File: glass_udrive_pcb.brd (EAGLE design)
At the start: 8.5 x 19 mm, 20 parts

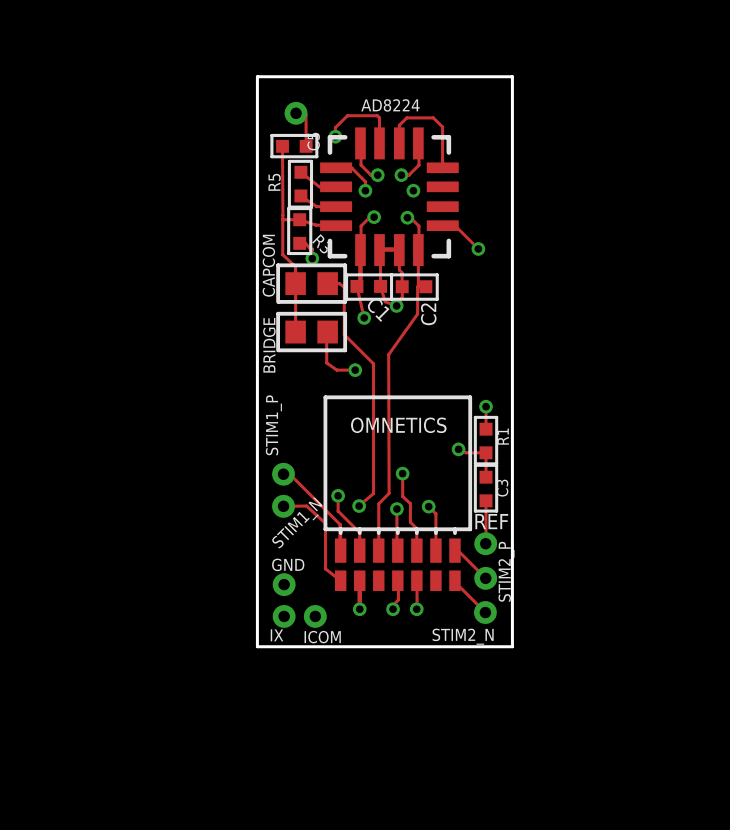
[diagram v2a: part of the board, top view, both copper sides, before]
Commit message: 1-Incorporating Michael Stetner's comments: ====================================================== 1. Move vias carrying output signals away from the corners of the AD8224. According to the datasheet (bottom of p. 22), vias should not be placed under the corners of the chip. 2. If you have enough space, add a 10 uF bypass capacitor on each supply, as suggested by the datasheet. These can be far from the AD8224. 3. Add a through hole for GND. This hole will be used during surgery to solder the ground wire that you put under the bird's skull. You already have one GND through hole, but that will be in use by the motor. 4. Remove the vias for +15V and -15V that are underneath the AD8224. Just run those two of the traces on the top side of the board. 5. Change capacitance of C1-C2 to 0.1 uF, per the datasheet 6. Remove the trace between the reference pads of the AD8224. This creates a loop in your ground, and loops pick up electromagnetic interference. 7. Add an orientation marker for the AD8224 on the silkscreen 8. On the bill of materials, fix the device name for the AD8224 (it says AD8424). 9. Increase the width of the traces for Ix, ICOM, +15V, and -15V. A wider trace will have a lower resistance, which is especially important for these traces that will be carrying the most current. ====================================================== 2-Redesigned and re-routed to match the available componenets' package sizes. 3-Added the headplate structure with thru-holes 4- fixed the dimension layer
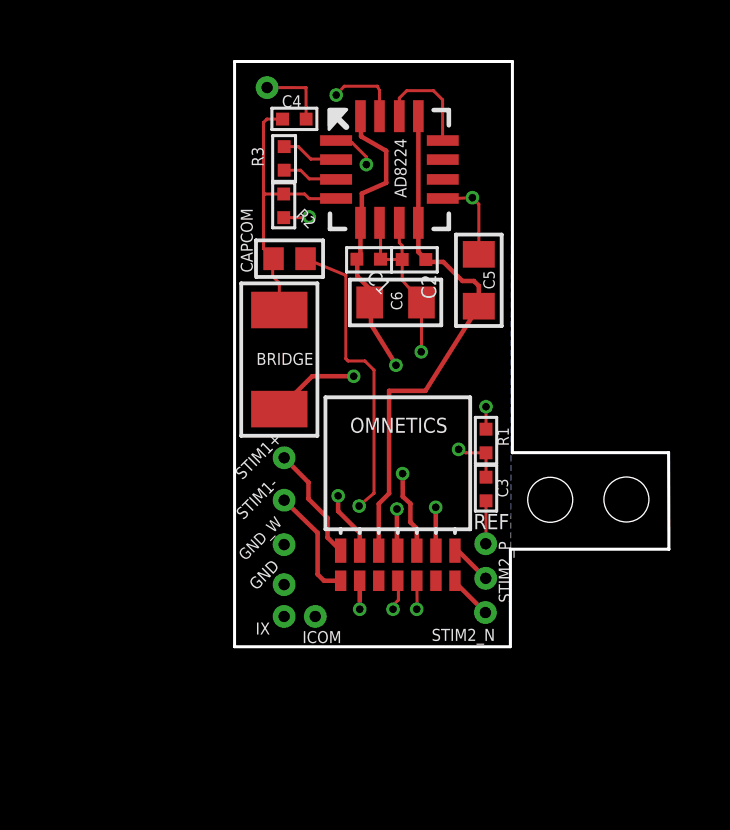
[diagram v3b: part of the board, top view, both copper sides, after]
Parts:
- removed R5: 5.49KOhm, GFL:0201
- removed STIM1_N, STIM1_P: (no value), GFL:30MIL/15MIL
- added C4: 6800pF, GFL:0201
- added C6: 10uF, GFL:0603
- added GND_W, STIM1+, STIM1-: (no value), GFL:30MIL/15MIL
- added R2: 10Mohm, GFL:0201
- BRIDGE: device GFL:0402 -> GFL:1206
- C1, C2: value .01uF -> 0.1uF
- C5: value 6800pF -> 10uF; device GFL:0201 -> GFL:0603
- R3: value 10Mohm -> 5.49KOhm
- moved C5 7.60 mm to (7.38, 12.2), turned to 270 degrees
- moved R3 2.49 mm to (0.89, 16.3)
- moved BRIDGE 1.42 mm to (0.73, 9.57), turned to 270 degrees
- moved GLASS 1.29 mm to (0.32, 18.6)
- moved CAPCOM 1.11 mm to (1.07, 12.9)
- moved AD8224 0.91 mm to (4.40, 15.9)
- moved C1 0.91 mm to (3.71, 12.9)
- moved C2 0.91 mm to (5.22, 12.9)
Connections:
- net +15V: now also C6.2
- net -15V: now also C5.2
- net GLASS: now also C4.1; no longer C5.1
- net GLASS_FLT: now also C4.2, R2.2; no longer C5.2, R3.2
- net GND: now also C5.1, C6.1, GND_W.P$1, R2.1; no longer R3.1
- net N$2: now also R3.2; no longer R5.2
- net N$4: now also R3.1; no longer R5.1
- net STIM1_N: now also STIM1-.P$1; no longer STIM1_N.P$1
- net STIM1_P: now also STIM1+.P$1; no longer STIM1_P.P$1
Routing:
- net GND: track 9.82 -> 13.0 mm
- net -15V: track 15.7 -> 17.7 mm, vias 2 -> 0
- net CAP_COM: track 13.0 -> 14.5 mm
- net GLASS_FLT: track 8.18 -> 9.68 mm
- net GLASS_OUT: track 20.5 -> 21.7 mm
- net GLASS: track 1.39 -> 2.35 mm
- net BRG_BAL: track 12.0 -> 12.7 mm
- net N$4: track 1.28 -> 1.86 mm
- net N$2: track 1.34 -> 1.91 mm
- net +15V: track 17.0 -> 16.8 mm, vias 4 -> 2
- net REF_FLT: track 14.0 -> 14.1 mm, vias 3 -> 2
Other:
- board size 8.5 x 19 mm -> 14.5 x 19.5 mm

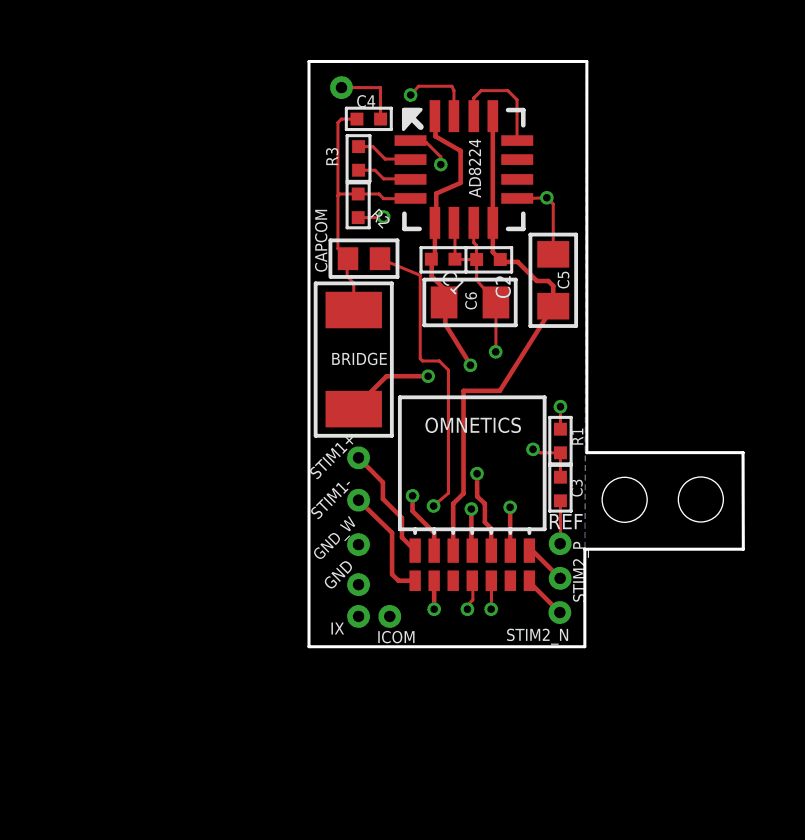
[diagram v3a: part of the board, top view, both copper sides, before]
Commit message: extended drive length to give more space at the bottom for dental cement anchoring. PCB = 9.26mm X 19.91 mm
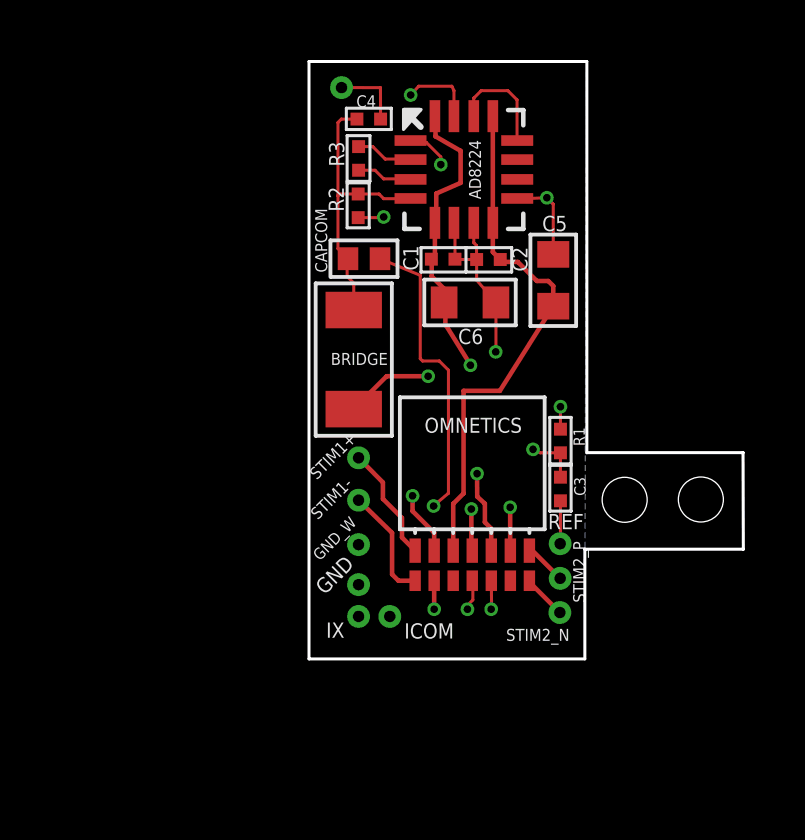
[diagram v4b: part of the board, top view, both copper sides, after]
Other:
- board size 14.5 x 19.5 mm -> 14.5 x 19.9 mm
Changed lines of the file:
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@@
 <board>
 <plain>
-<wire x1="-0.762" y1="0" x2="8.4328" y2="0" width="0.1" layer="20"/>
+<wire x1="-0.762" y1="-0.4064" x2="8.4328" y2="-0.4064" width="0.1" layer="20"/>
 <wire x1="8.5" y1="6.4636" x2="8.5" y2="19.508" width="0.1" layer="20"/>
 <wire x1="8.5" y1="19.508" x2="-0.762" y2="19.508" width="0.1" layer="20"/>
-<wire x1="-0.762" y1="19.508" x2="-0.762" y2="0" width="0.1" layer="20"/>
+<wire x1="-0.762" y1="19.508" x2="-0.762" y2="-0.4064" width="0.1" layer="20"/>
 <text x="7.2" y="8.1" size="0.5" layer="22" font="vector" rot="MR270">Nader Nikbakht
 FeeLab, MIT 2018</text>
@@
 </polygon>
 <wire x1="2.6816" y1="17.6058" x2="2.961" y2="17.3264" width="0.2032" layer="21"/>
-<wire x1="8.4328" y1="0" x2="8.4328" y2="3.2512" width="0.1016" layer="20"/>
+<wire x1="8.4328" y1="-0.4064" x2="8.4328" y2="3.2512" width="0.1016" layer="20"/>
 <wire x1="8.4328" y1="3.2512" x2="13.716" y2="3.2512" width="0.1016" layer="20"/>
 <wire x1="13.716" y1="3.2512" x2="13.706" y2="6.47" width="0.1016" layer="20"/>
 <wire x1="8.4944" y1="6.47" x2="13.706" y2="6.47" width="0.1016" layer="20"/>
-<dimension x1="8.4328" y1="0" x2="8.4328" y2="3.2512" x3="18.796" y3="1.6256" textsize="0.5" layer="20" width="0.01"/>
+<dimension x1="8.4328" y1="0" x2="8.4328" y2="3.2512" x3="18.796" y3="1.6256" textsize="0.5" layer="20" width="0.01" visible="yes"/>
 <hole x="9.76" y="4.898" drill="1.5"/>
 <hole x="12.3" y="4.908" drill="1.5"/>
-<dimension x1="9.76" y1="4.4" x2="12.3" y2="4.4" x3="11.03" y3="6.988" textsize="0.5" layer="20" dtype="diameter" width="0.01" extwidth="0.01"/>
-<dimension x1="13.716" y1="5.588" x2="8.5044" y2="5.588" x3="11.1102" y3="8.124" textsize="0.5" layer="20" width="0.01" extwidth="0.01"/>
-<dimension x1="-0.762" y1="0" x2="13.716" y2="0" x3="6.477" y3="-1.778" textsize="0.5" layer="20" width="0.01" extwidth="0.01"/>
-<dimension x1="13.716" y1="3.2512" x2="13.706" y2="6.47" x3="14.5544" y3="4.86321875" textsize="0.5" layer="20" width="0.01" extwidth="0.01"/>
-<dimension x1="-0.762" y1="0" x2="-0.762" y2="19.508" x3="-2.1844" y3="9.754" textsize="0.5" layer="20" width="0.01" extwidth="0.01"/>
-<dimension x1="8.5" y1="19.508" x2="-0.762" y2="19.508" x3="3.869" y3="21.463" textsize="0.5" layer="20" width="0.01" extwidth="0.01"/>
+<dimension x1="9.76" y1="4.4" x2="12.3" y2="4.4" x3="11.03" y3="6.988" textsize="0.5" layer="20" dtype="diameter" width="0.01" extwidth="0.01" visible="yes"/>
+<dimension x1="13.716" y1="5.588" x2="8.5044" y2="5.588" x3="11.1102" y3="8.124" textsize="0.5" layer="20" width="0.01" extwidth="0.01" visible="yes"/>
+<dimension x1="-0.762" y1="0" x2="13.716" y2="0" x3="6.477" y3="-1.778" textsize="0.5" layer="20" width="0.01" extwidth="0.01" visible="yes"/>
+<dimension x1="13.716" y1="3.2512" x2="13.706" y2="6.47" x3="14.5544" y3="4.86321875" textsize="0.5" layer="20" width="0.01" extwidth="0.01" visible="yes"/>
+<dimension x1="8.5" y1="19.508" x2="-0.762" y2="19.508" x3="3.869" y3="21.463" textsize="0.5" layer="20" width="0.01" extwidth="0.01" visible="yes"/>
+<dimension x1="-0.762" y1="-0.4064" x2="-0.762" y2="19.508" x3="-2.2352" y3="9.5508" textsize="0.508" layer="20" width="0.01" extwidth="0.01" visible="yes"/>
 </plain>
 <attributes>
@@
 <elements>
 <element name="C1" library="GFL" package="0201" value="0.1uF" x="3.71" y="12.918" smashed="yes" rot="R180">
-<attribute name="NAME" x="4.5114" y="12.0496" size="0.5" layer="25" font="vector" rot="R135"/>
+<attribute name="NAME" x="2.8856" y="12.5378" size="0.508" layer="25" font="vector" rot="R90"/>
 <attribute name="VALUE" x="4.98" y="14.696" size="0.762" layer="27" font="vector" ratio="12" rot="R180"/>
 </element>
 <element name="C2" library="GFL" package="0201" value="0.1uF" x="5.22" y="12.908" smashed="yes">
-<attribute name="NAME" x="5.961" y="11.5902" size="0.5" layer="25" font="vector" ratio="12" rot="R90"/>
+<attribute name="NAME" x="6.5198" y="12.5046" size="0.5" layer="25" font="vector" ratio="12" rot="R90"/>
 <attribute name="VALUE" x="3.95" y="11.13" size="0.762" layer="27" font="vector" ratio="12"/>
 </element>
@@
 </element>
 <element name="ICOM" library="GFL" package="30MIL/15MIL" value="" x="1.93" y="1.01" smashed="yes">
-<attribute name="NAME" x="1.498" y="0.1212" size="0.4" layer="25" font="vector" ratio="12"/>
+<attribute name="NAME" x="2.4124" y="0.2736" size="0.508" layer="25" font="vector" ratio="12"/>
 <attribute name="VALUE" x="0.7108" y="-0.5521" size="0.762" layer="27" font="vector" ratio="12"/>
 </element>
 <element name="IX" library="GFL" package="30MIL/15MIL" value="" x="0.89" y="1.01" smashed="yes">
-<attribute name="NAME" x="0.4214" y="0.8074" size="0.4" layer="25" font="vector" ratio="12" rot="R180"/>
+<attribute name="NAME" x="0.4214" y="0.8074" size="0.508" layer="25" font="vector" ratio="12" rot="R180"/>
 <attribute name="VALUE" x="-0.3292" y="-0.5521" size="0.762" layer="27" font="vector" ratio="12"/>
 </element>
@@
 </element>
 <element name="GND" library="GFL" package="30MIL/15MIL" value="" x="0.89" y="2.07" smashed="yes">
-<attribute name="NAME" x="-0.0396" y="1.8582" size="0.4" layer="25" font="vector" ratio="12" rot="R45"/>
+<attribute name="NAME" x="-0.2428" y="1.7058" size="0.508" layer="25" font="vector" ratio="12" rot="R45"/>
 <attribute name="VALUE" x="-0.3292" y="0.5079" size="0.762" layer="27" font="vector" ratio="12"/>
 </element>
@@
 <attribute name="MPN" value="AD8426ACPZ-R7" x="4.4" y="15.908" size="1.778" layer="27" display="off"/>
 <attribute name="OC_NEWARK" value="58T4523" x="4.4" y="15.908" size="1.778" layer="27" display="off"/>
-<attribute name="NAME" x="4.9708" y="14.9664" size="0.4" layer="25" ratio="10" rot="SR90"/>
+<attribute name="NAME" x="4.9708" y="14.9156" size="0.4" layer="25" font="vector" ratio="10" rot="SR90"/>
 <attribute name="VALUE" x="0.9456" y="9.431" size="2.0828" layer="27" ratio="10" rot="SR0"/>
 </element>
@@
 </element>
 <element name="R3" library="GFL" package="0201" value="5.49KOhm" x="0.8912" y="16.2772" smashed="yes" rot="R90">
-<attribute name="NAME" x="0.2098" y="16.0054" size="0.4" layer="25" font="vector" rot="R90"/>
+<attribute name="NAME" x="0.413" y="16.0054" size="0.508" layer="25" font="vector" rot="R90"/>
 <attribute name="VALUE" x="2.7962" y="15.6422" size="1.27" layer="27" rot="R90"/>
 </element>
 <element name="R2" library="GFL" package="0201" value="10Mohm" x="0.8766" y="14.6972" smashed="yes" rot="R90">
-<attribute name="NAME" x="2.0046" y="14.1798" size="0.4" layer="25" rot="R135"/>
+<attribute name="NAME" x="0.3998" y="14.5014" size="0.508" layer="25" font="vector" rot="R90"/>
 <attribute name="VALUE" x="2.7816" y="14.0622" size="1.27" layer="27" rot="R90"/>
 </element>
@@
 </element>
 <element name="R1" library="GFL" package="0201" value="10Mohm" x="7.62" y="6.858" smashed="yes" rot="R270">
-<attribute name="NAME" x="8.001" y="7.3152" size="0.381" layer="25" font="vector" rot="R270"/>
+<attribute name="NAME" x="8.0518" y="7.3152" size="0.381" layer="25" font="vector" rot="R270"/>
 <attribute name="VALUE" x="6.0452" y="8.0518" size="1.016" layer="27" font="vector" rot="R270"/>
 </element>
 <element name="C3" library="GFL" package="0201" value="6800pF" x="7.62" y="5.2578" smashed="yes" rot="R90">
-<attribute name="NAME" x="8.3566" y="4.9784" size="0.381" layer="25" font="vector" rot="R90"/>
+<attribute name="NAME" x="8.4582" y="5.0292" size="0.381" layer="25" font="vector" rot="R90"/>
 <attribute name="VALUE" x="9.1948" y="4.064" size="1.016" layer="27" font="vector" rot="R90"/>
 </element>
 <element name="C6" library="GFL" package="0603" value="10uF" x="4.6052" y="11.476" smashed="yes" rot="R180">
-<attribute name="NAME" x="4.4498" y="11.8442" size="0.381" layer="25" font="vector" rot="R270"/>
+<attribute name="NAME" x="4.2086" y="10.0886" size="0.508" layer="25" font="vector"/>
 <attribute name="VALUE" x="5.799" y="13.0508" size="1.016" layer="27" font="vector" rot="R180"/>
 </element>
 <element name="C5" library="GFL" package="0603" value="10uF" x="7.38" y="12.215" smashed="yes" rot="R270">
-<attribute name="NAME" x="7.9108" y="11.915" size="0.381" layer="25" font="vector" rot="R90"/>
+<attribute name="NAME" x="7.8462" y="14.3624" size="0.508" layer="25" font="vector" rot="R180"/>
 <attribute name="VALUE" x="5.8052" y="13.4088" size="1.016" layer="27" font="vector" rot="R270"/>
 </element>
@@
 <vertex x="-0.762" y="19.508"/>
 <vertex x="8.49" y="19.498"/>
-<vertex x="8.43" y="0"/>
-<vertex x="-0.762" y="0"/>
+<vertex x="8.43" y="-0.4064"/>
+<vertex x="-0.762" y="-0.4064"/>
 </polygon>
 <contactref element="C2" pad="1"/>

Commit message: solved the order of CAPCOM and Bridge balance nets and routing as per GFL suggestions.
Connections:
- net GLASS: now also BRIDGE.1, CAPCOM.1
- net GLASS_FLT: no longer BRIDGE.1, CAPCOM.1
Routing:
- net GLASS: track 2.35 -> 12.3 mm
- net GLASS_FLT: track 9.68 -> 7.39 mm
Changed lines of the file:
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@@
 <wire x1="0.3222" y1="18.6384" x2="1.62" y2="18.6366" width="0.1016" layer="1"/>
 <wire x1="1.62" y1="18.6366" x2="1.6237" y2="17.588" width="0.1016" layer="1"/>
+<contactref element="BRIDGE" pad="1"/>
+<wire x1="0.729678125" y1="11.22309375" x2="0.7112" y2="11.22309375" width="0.1524" layer="1"/>
+<wire x1="0.7112" y1="11.22309375" x2="0.7112" y2="9.5504" width="0.1524" layer="1"/>
+<contactref element="CAPCOM" pad="1"/>
+<wire x1="0.729678125" y1="11.22309375" x2="0.53710625" y2="11.22309375" width="0.1524" layer="1"/>
+<wire x1="0.53710625" y1="11.22309375" x2="0.53710625" y2="12.9356" width="0.1524" layer="1"/>
+<wire x1="0.53710625" y1="12.9356" x2="0.2216" y2="12.9356" width="0.1524" layer="1"/>
+<wire x1="0.2216" y1="12.9356" x2="-0.1524" y2="13.3096" width="0.1524" layer="1"/>
+<wire x1="-0.1524" y1="13.3096" x2="-0.1524" y2="18.1638" width="0.1524" layer="1"/>
+<wire x1="-0.1524" y1="18.1638" x2="0.3222" y2="18.6384" width="0.1524" layer="1"/>
 </signal>
 <signal name="GLASS_OUT">
@@
 </signal>
 <signal name="GLASS_FLT">
-<contactref element="CAPCOM" pad="1"/>
-<contactref element="BRIDGE" pad="1"/>
 <contactref element="AD8224" pad="4"/>
 <contactref element="R2" pad="2"/>
@@
 <wire x1="0.2032" y1="17.4752" x2="0.2032" y2="15.0368" width="0.1016" layer="1"/>
 <wire x1="0.2032" y1="15.0368" x2="0.2032" y2="13.26950625" width="0.1016" layer="1"/>
-<wire x1="0.2032" y1="13.26950625" x2="0.53710625" y2="12.9356" width="0.1016" layer="1"/>
 <wire x1="0.8766" y1="15.0909" x2="0.2573" y2="15.0909" width="0.1016" layer="1"/>
 <wire x1="0.2573" y1="15.0909" x2="0.2032" y2="15.0368" width="0.1016" layer="1"/>
@@
 <wire x1="1.7272" y1="14.9352" x2="2.6144" y2="14.9352" width="0.1016" layer="1"/>
 <wire x1="2.6144" y1="14.9352" x2="2.622" y2="14.9428" width="0.1016" layer="1"/>
-<wire x1="0.729678125" y1="11.22309375" x2="0.729678125" y2="12.122721875" width="0.1016" layer="1"/>
-<wire x1="0.729678125" y1="12.122721875" x2="0.508" y2="12.3444" width="0.1016" layer="1"/>
-<wire x1="0.508" y1="12.3444" x2="0.508" y2="12.90649375" width="0.1016" layer="1"/>
-<wire x1="0.508" y1="12.90649375" x2="0.53710625" y2="12.9356" width="0.1016" layer="1"/>
 </signal>
 <signal name="REF_FLT">
